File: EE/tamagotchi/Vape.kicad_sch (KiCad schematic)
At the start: 12 parts, among them J1 Conn_01x02_Male, Q4 Q_NMOS_GSD, Q5 Q_PMOS_GSD, SW2 TL1260BQRBLK

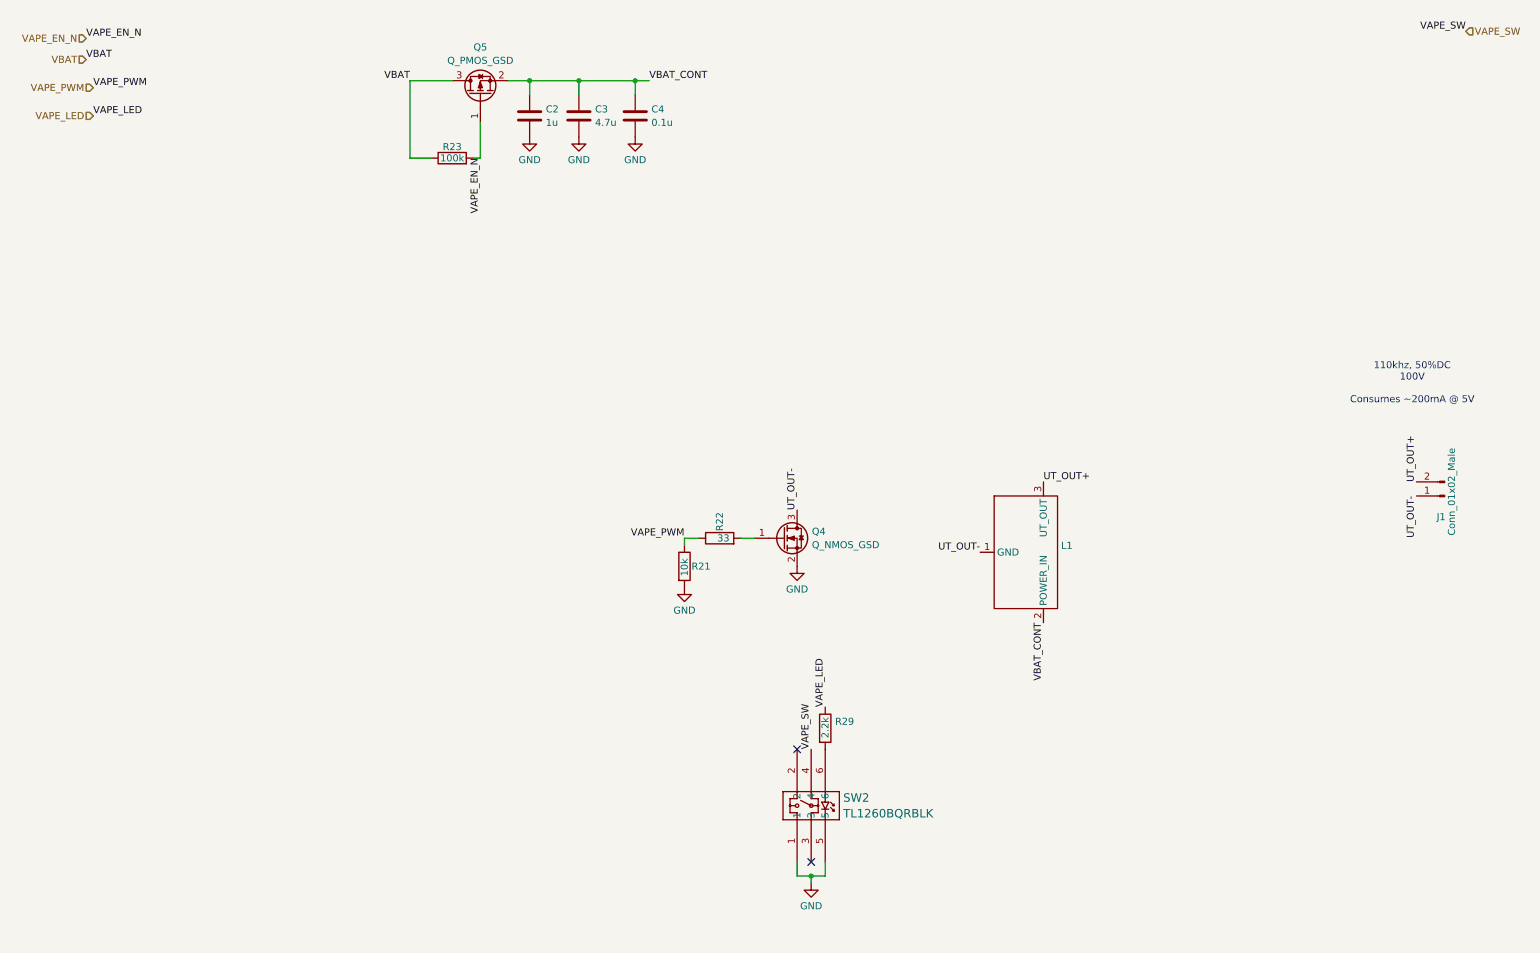
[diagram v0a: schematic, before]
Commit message: WIP - Overall Cleanup, Power Change
Added expected loads for power in schematic.
Changed power arch to use existing design that appears to work.
Removed rear backlight LEDs - shouldn't be necessary.
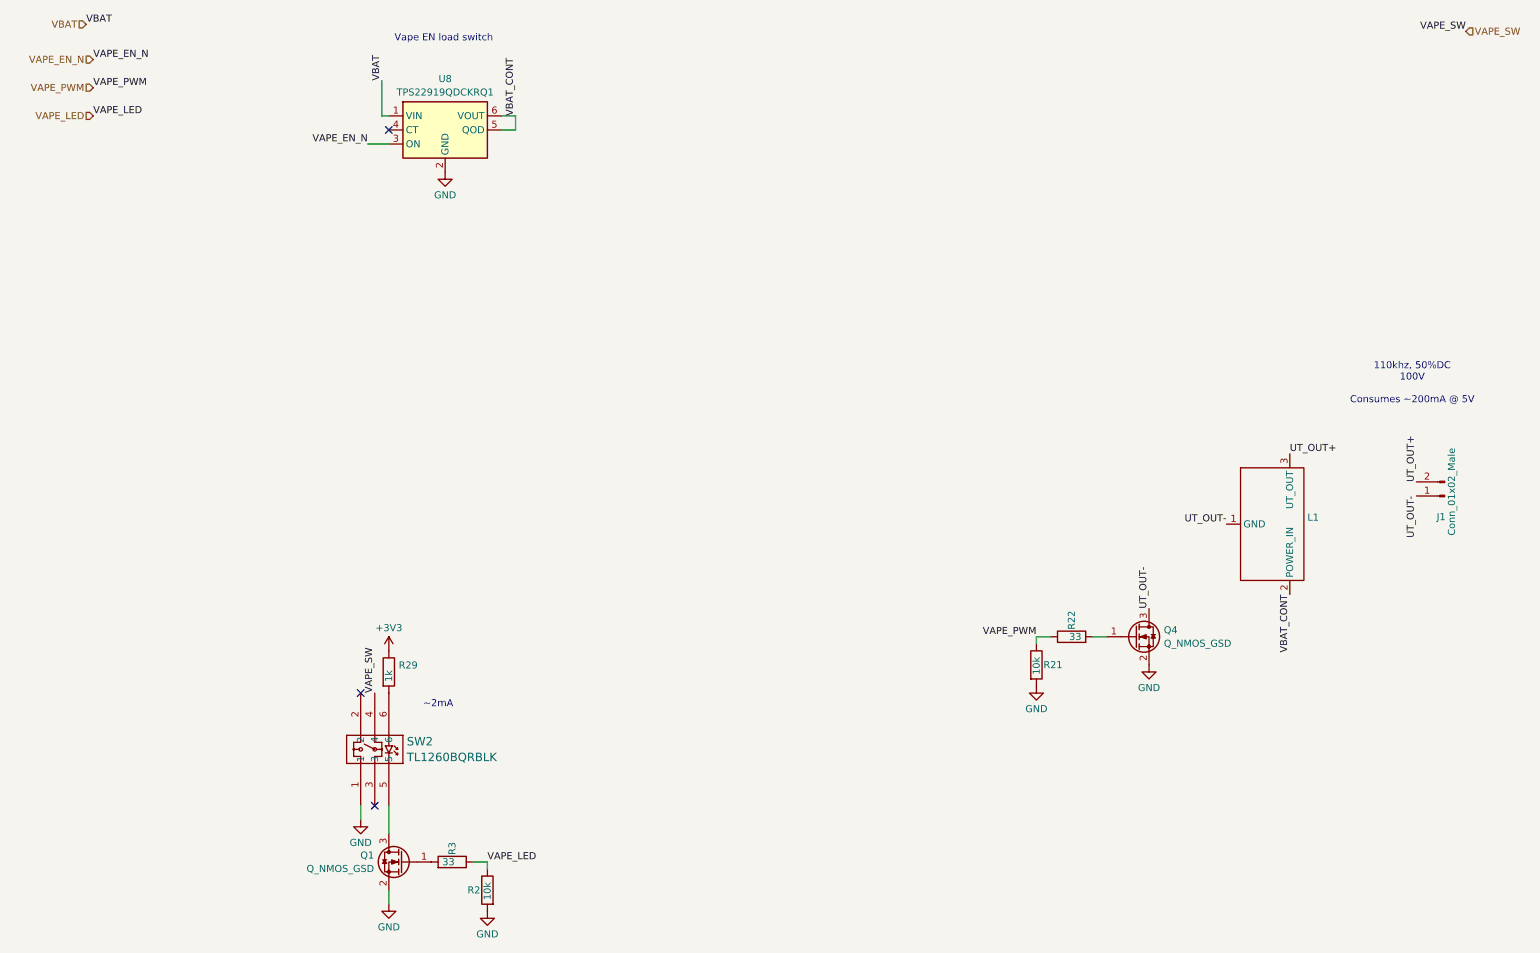
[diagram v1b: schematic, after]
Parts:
- removed C2: 1u, Capacitor_SMD:C_0402_1005Metric_Pad0.74x0.62mm_HandSolder, symbol Device:C
- removed C3: 4.7u, Capacitor_SMD:C_0402_1005Metric_Pad0.74x0.62mm_HandSolder, symbol Device:C
- removed C4: 0.1u, Capacitor_SMD:C_0402_1005Metric_Pad0.74x0.62mm_HandSolder, symbol Device:C
- removed Q5: Q_PMOS_GSD, Package_TO_SOT_SMD:SOT-23, symbol Transistor_FET:Q_PMOS_GSD
- removed R23: 100k, Resistor_SMD:R_0402_1005Metric_Pad0.72x0.64mm_HandSolder, symbol Device:R
- added Q1: Q_NMOS_GSD, Package_TO_SOT_SMD:SOT-23, symbol Transistor_FET:Q_NMOS_GSD
- added R2: 10k, Resistor_SMD:R_0402_1005Metric_Pad0.72x0.64mm_HandSolder, symbol Device:R
- added R3: 33, Resistor_SMD:R_0402_1005Metric_Pad0.72x0.64mm_HandSolder, symbol Device:R
- added U8: TPS22919QDCKRQ1, Package_TO_SOT_SMD:SOT-363_SC-70-6, symbol Power_Management:TPS22917DBV
- R29: value 2.2k -> 1k
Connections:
- net GND: now also Q1.2 (S), R2.2, U8.2 (GND); no longer SW2.5
- net VAPE_EN_N: now also U8.3 (ON)
- net VAPE_LED: now also R2.1, R3.1; no longer R29.1
- net VBAT: now also U8.1 (VIN)
- net VBAT_CONT: now also U8.5 (QOD), U8.6 (VOUT)
- new net: Q1.1 (G), R3.2
- new net: Q1.3 (D), SW2.5
- new net +3V3: R29.1
- no-connect marks 2 -> 3
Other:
- note added: "Vape EN load switch"
- note added: "~2mA"
- moved on the sheet: L1, Q4, R21, R22, R29, SW2
